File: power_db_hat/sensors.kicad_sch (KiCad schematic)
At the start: 14 parts, among them U1 INA3221

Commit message: update
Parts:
- removed R9: 0, symbol Device:R_US
- added JP1: SolderJumper_2_Open, Jumper:SolderJumper-2_P1.3mm_Open_TrianglePad1.0x1.5mm, symbol Jumper:SolderJumper_2_Open
- C3: footprint (none) -> Capacitor_SMD:C_0805_2012Metric_Pad1.18x1.45mm_HandSolder
- R32, R35, R36, R37, R38, R39, R40, R41: footprint (none) -> Resistor_SMD:R_0603_1608Metric_Pad0.98x0.95mm_HandSolder
- R33: value 10mR -> 10m; footprint (none) -> Resistor_SMD:R_2512_6332Metric_Pad1.40x3.35mm_HandSolder
- R34, R8: footprint (none) -> Resistor_SMD:R_2512_6332Metric_Pad1.40x3.35mm_HandSolder
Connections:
- net VDD: now also JP1.1 (A)
- net at U1.4 (VS): now also JP1.2 (B)
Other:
- moved on the sheet: C3
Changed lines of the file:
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@@
 	(text_box "Channel 1: 24V, 10A max (1W dissipation)\n- shunt value: 10mR\n- recommended footprint: 2512 (2W)\n\nChannel 2: 12V, 5A max (1w dissipation)\n- shunt value: 10mR\n- recommended footprint: 2512 (2W)\n\nChannel 3: 5V, 5A max (250mW dissipation)\n- shunt value 10mW\n- recommended footprint: 2512 (1W)"
 		(exclude_from_sim no)
-		(at 71.755 88.9 0)
+		(at 17.78 17.78 0)
 		(size 44.45 29.21)
 		(margins 0.9525 0.9525 0.9525 0.9525)
@@
 	(wire
 		(pts
+			(xy 71.12 43.18) (xy 72.39 43.18)
+		)
+		(stroke
+			(width 0)
+			(type default)
+		)
+	)
+	(wire
+		(pts
 			(xy 50.8 53.34) (xy 59.69 53.34)
 		)
@@
 	(wire
 		(pts
-			(xy 73.66 35.56) (xy 78.74 35.56)
+			(xy 71.12 35.56) (xy 78.74 35.56)
 		)
 		(stroke
@@
 	(hierarchical_label "VDD"
 		(shape input)
-		(at 73.66 35.56 90)
+		(at 71.12 35.56 90)
 		(effects
 			(font
@@
 	(symbol
 		(lib_id "Device:C")
-		(at 73.66 39.37 0)
+		(at 71.12 39.37 0)
 		(unit 1)
 		(exclude_from_sim no)
@@
 		(fields_autoplaced yes)
 		(property "Reference" "C3"
-			(at 77.47 38.0999 0)
+			(at 74.93 38.0999 0)
 			(effects
 				(font
@@
 		)
 		(property "Value" "100nF"
-			(at 77.47 40.6399 0)
+			(at 74.93 40.6399 0)
 			(effects
 				(font
@@
 			)
 		)
-		(property "Footprint" ""
-			(at 74.6252 43.18 0)
+		(property "Footprint" "Capacitor_SMD:C_0805_2012Metric_Pad1.18x1.45mm_HandSolder"
+			(at 72.0852 43.18 0)
 			(effects
 				(font
@@
 		)
 		(property "Datasheet" "~"
-			(at 73.66 39.37 0)
+			(at 71.12 39.37 0)
 			(effects
 				(font
@@
 		)
 		(property "Description" "Unpolarized capacitor"
-			(at 73.66 39.37 0)
+			(at 71.12 39.37 0)
 			(effects
 				(font
@@
 		)
 		(instances
-			(project ""
+			(project "power_db_hat"
 				(path "/e63e39d7-6ac0-4ffd-8aa3-1841a4541b55/fd5e5e33-5dc6-45b9-b42d-1fb287c03766/49be27b4-9dd5-4ba8-9fd8-2a64f398149b"
 					(reference "#PWR09")
@@
 			)
 		)
-		(property "Footprint" ""
+		(property "Footprint" "Resistor_SMD:R_0603_1608Metric_Pad0.98x0.95mm_HandSolder"
 			(at 126.746 54.864 90)
 			(effects
@@
 			)
 		)
-		(property "Footprint" ""
+		(property "Footprint" "Resistor_SMD:R_0603_1608Metric_Pad0.98x0.95mm_HandSolder"
 			(at 112.776 72.136 90)
 			(effects
@@
 			)
 		)
-		(property "Footprint" ""
+		(property "Footprint" "Resistor_SMD:R_0603_1608Metric_Pad0.98x0.95mm_HandSolder"
 			(at 144.526 62.484 90)
 			(effects
@@
 			)
 		)
-		(property "Footprint" ""
+		(property "Footprint" "Resistor_SMD:R_2512_6332Metric_Pad1.40x3.35mm_HandSolder"
 			(at 63.246 72.136 90)
 			(effects
@@
 			)
 		)
-		(property "Footprint" ""
+		(property "Footprint" "Resistor_SMD:R_2512_6332Metric_Pad1.40x3.35mm_HandSolder"
 			(at 63.246 56.896 90)
 			(effects
@@
 			)
 		)
-		(property "Footprint" ""
+		(property "Footprint" "Resistor_SMD:R_0603_1608Metric_Pad0.98x0.95mm_HandSolder"
 			(at 108.966 77.216 90)
 			(effects
@@
 	)
 	(symbol
+		(lib_id "Jumper:SolderJumper_2_Open")
+		(at 82.55 35.56 0)
+		(unit 1)
+		(exclude_from_sim no)
+		(in_bom no)
+		(on_board yes)
+		(dnp no)
+		(property "Reference" "JP1"
+			(at 82.55 32.004 0)
+			(effects
+				(font
+					(size 1.27 1.27)
+				)
+			)
+		)
+		(property "Value" "SolderJumper_2_Open"
+			(at 85.852 27.178 0)
+			(effects
+				(font
+					(size 1.27 1.27)
+				)
+				(hide yes)
+			)
+		)
+		(property "Footprint" "Jumper:SolderJumper-2_P1.3mm_Open_TrianglePad1.0x1.5mm"
+			(at 82.55 35.56 0)
+			(effects
+				(font
+					(size 1.27 1.27)
+				)
+				(hide yes)
+			)
+		)
+		(property "Datasheet" "~"
+			(at 82.55 35.56 0)
+			(effects
+				(font
+					(size 1.27 1.27)
+				)
+				(hide yes)
+			)
+		)
+		(property "Description" "Solder Jumper, 2-pole, open"
+			(at 82.55 35.56 0)
+			(effects
+				(font
+					(size 1.27 1.27)
+				)
+				(hide yes)
+			)
+		)
+		(pin "1"
+		)
+		(pin "2"
+		)
+		(instances
+			(project "power_db_hat"
+				(path "/e63e39d7-6ac0-4ffd-8aa3-1841a4541b55/fd5e5e33-5dc6-45b9-b42d-1fb287c03766/49be27b4-9dd5-4ba8-9fd8-2a64f398149b"
+					(reference "JP1")
+					(unit 1)
+				)
+			)
+		)
+	)
+	(symbol
 		(lib_id "power:GND")
-		(at 73.66 43.18 0)
+		(at 72.39 43.18 0)
 		(unit 1)
 		(exclude_from_sim no)
@@
 		(fields_autoplaced yes)
 		(property "Reference" "#PWR035"
-			(at 73.66 49.53 0)
+			(at 72.39 49.53 0)
 			(effects
 				(font
@@
 		)
 		(property "Value" "GND"
-			(at 73.66 48.26 0)
+			(at 72.39 48.26 0)
 			(effects
 				(font
@@
 		)
 		(property "Footprint" ""
-			(at 73.66 43.18 0)
+			(at 72.39 43.18 0)
 			(effects
 				(font
@@
 		)
 		(property "Datasheet" ""
-			(at 73.66 43.18 0)
+			(at 72.39 43.18 0)
 			(effects
 				(font
@@
 		)
 		(property "Description" "Power symbol creates a global label with name \"GND\" , ground"
-			(at 73.66 43.18 0)
+			(at 72.39 43.18 0)
 			(effects
 				(font
@@
 			)
 		)
-		(property "Footprint" ""
+		(property "Footprint" "Resistor_SMD:R_0603_1608Metric_Pad0.98x0.95mm_HandSolder"
 			(at 110.236 49.784 90)
 			(effects
@@
 			)
 		)
-		(property "Footprint" ""
+		(property "Footprint" "Resistor_SMD:R_0603_1608Metric_Pad0.98x0.95mm_HandSolder"
 			(at 153.416 65.024 90)
 			(effects
@@
 				(path "/e63e39d7-6ac0-4ffd-8aa3-1841a4541b55/fd5e5e33-5dc6-45b9-b42d-1fb287c03766/49be27b4-9dd5-4ba8-9fd8-2a64f398149b"
 					(reference "R36")
-					(unit 1)
-				)
-			)
-		)
-	)
-	(symbol
-		(lib_id "Device:R_US")
-		(at 82.55 35.56 90)
-		(unit 1)
-		(exclude_from_sim no)
-		(in_bom yes)
-		(on_board yes)
-		(dnp no)
-		(fields_autoplaced yes)
-		(property "Reference" "R9"
-			(at 82.55 29.21 90)
-			(effects
-				(font
-					(size 1.27 1.27)
-				)
-			)
-		)
-		(property "Value" "0"
-			(at 82.55 31.75 90)
-			(effects
-				(font
-					(size 1.27 1.27)
-				)
-			)
-		)
-		(property "Footprint" ""
-			(at 82.804 34.544 90)
-			(effects
-				(font
-					(size 1.27 1.27)
-				)
-				(hide yes)
-			)
-		)
-		(property "Datasheet" "~"
-			(at 82.55 35.56 0)
-			(effects
-				(font
-					(size 1.27 1.27)
-				)
-				(hide yes)
-			)
-		)
-		(property "Description" "Resistor, US symbol"
-			(at 82.55 35.56 0)
-			(effects
-				(font
-					(size 1.27 1.27)
-				)
-				(hide yes)
-			)
-		)
-		(pin "1"
-		)
-		(pin "2"
-		)
-		(instances
-			(project "power_db_hat"
-				(path "/e63e39d7-6ac0-4ffd-8aa3-1841a4541b55/fd5e5e33-5dc6-45b9-b42d-1fb287c03766/49be27b4-9dd5-4ba8-9fd8-2a64f398149b"
-					(reference "R9")
 					(unit 1)
 				)
@@
 			)
 		)
-		(property "Footprint" ""
+		(property "Footprint" "Resistor_SMD:R_0603_1608Metric_Pad0.98x0.95mm_HandSolder"
 			(at 119.126 52.324 90)
 			(effects
@@
 			)
 		)
-		(property "Value" "10mR"
+		(property "Value" "10m"
 			(at 55.88 64.77 90)
 			(effects
@@
 			)
 		)
-		(property "Footprint" ""
+		(property "Footprint" "Resistor_SMD:R_2512_6332Metric_Pad1.40x3.35mm_HandSolder"
 			(at 63.246 64.516 90)
 			(effects
@@
 			)
 		)
-		(property "Footprint" ""
+		(property "Footprint" "Resistor_SMD:R_0603_1608Metric_Pad0.98x0.95mm_HandSolder"
 			(at 134.366 57.404 90)
 			(effects

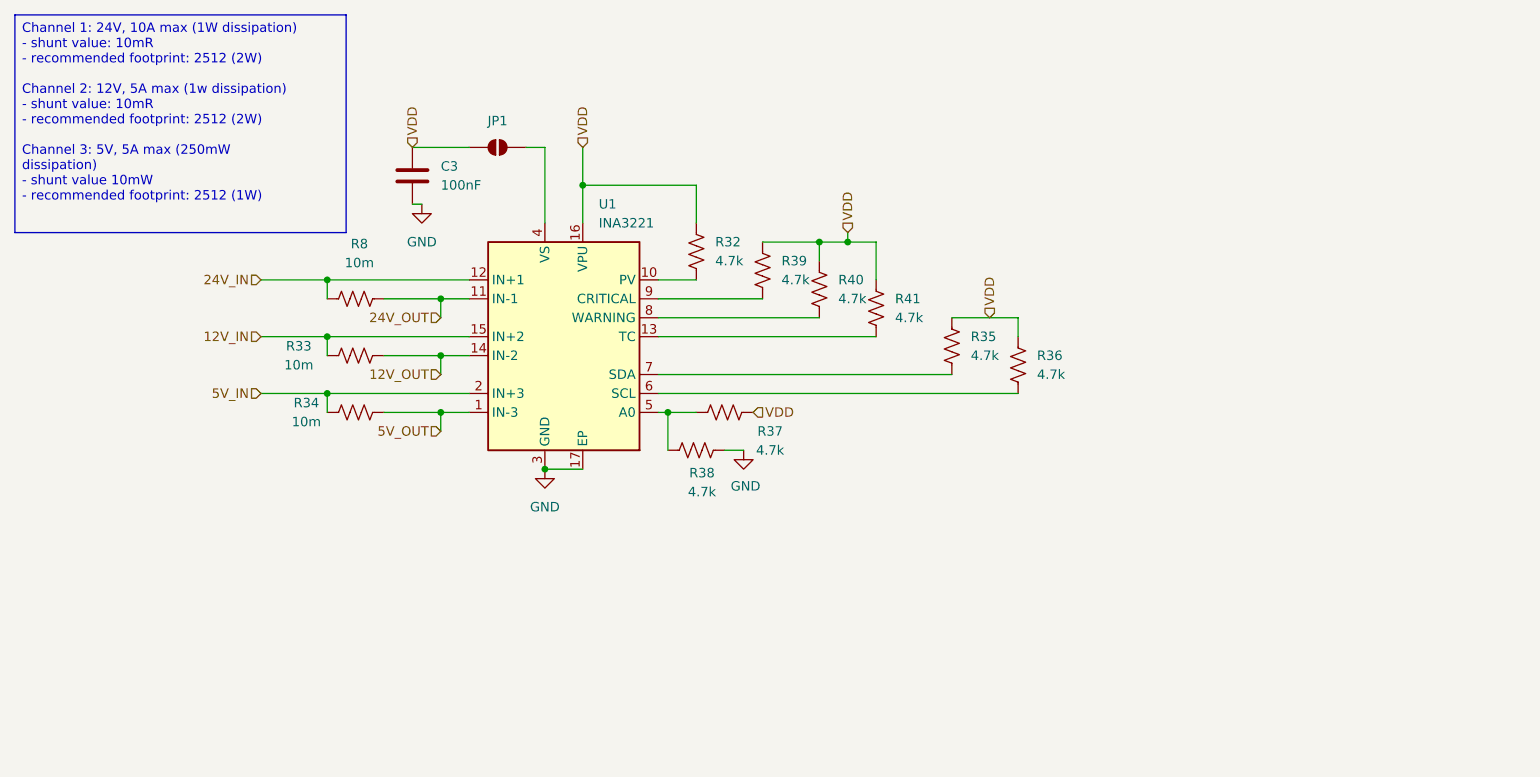
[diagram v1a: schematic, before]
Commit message: split into two PCBs
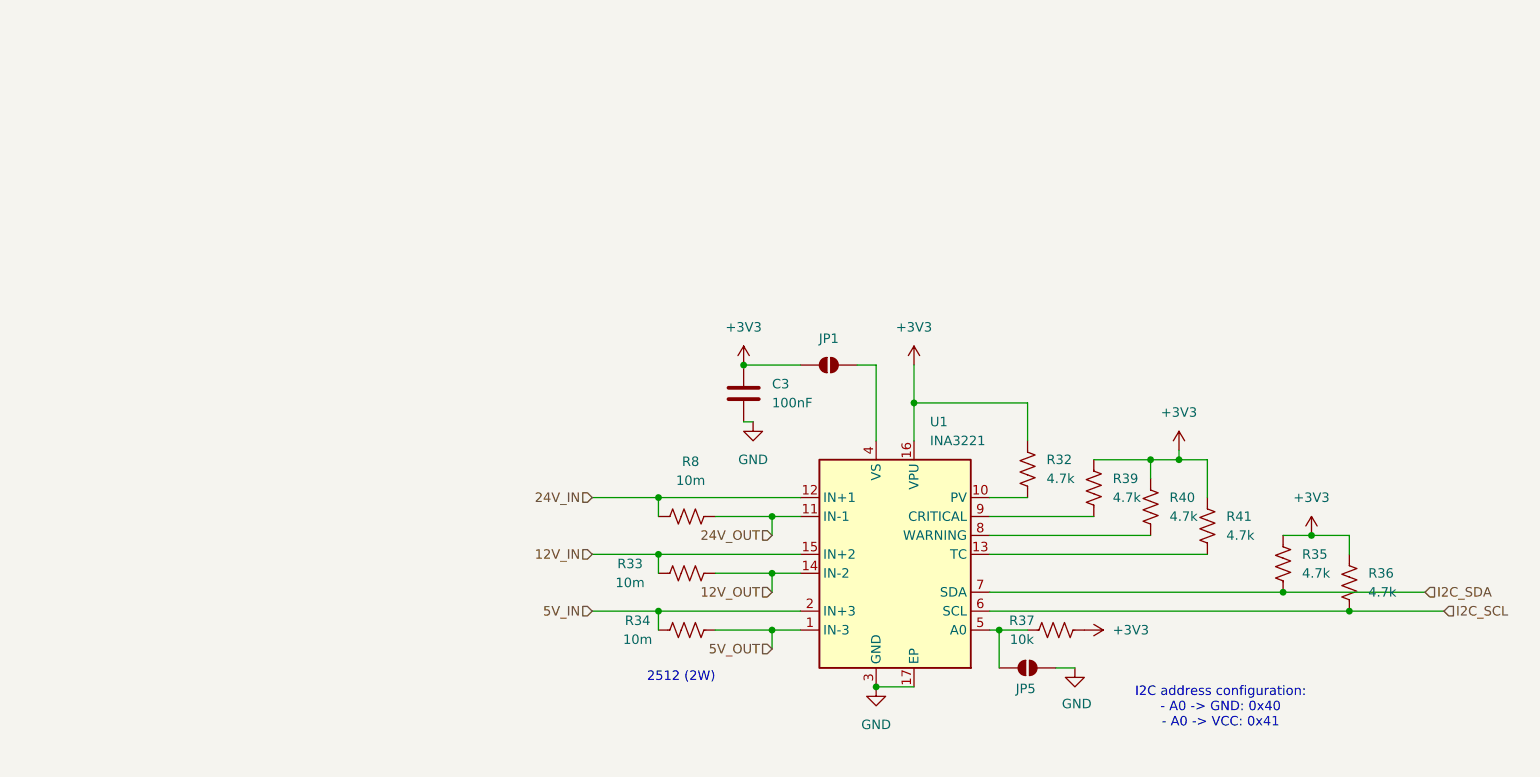
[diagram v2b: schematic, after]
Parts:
- removed R38: 4.7k, Resistor_SMD:R_0603_1608Metric_Pad0.98x0.95mm_HandSolder, symbol Device:R_US
- added JP5: SolderJumper_2_Open, Jumper:SolderJumper-2_P1.3mm_Open_TrianglePad1.0x1.5mm, symbol Jumper:SolderJumper_2_Open
- C3: footprint Capacitor_SMD:C_0805_2012Metric_Pad1.18x1.45mm_HandSolder -> Capacitor_SMD:C_0603_1608Metric_Pad1.08x0.95mm_HandSolder
- R37: value 4.7k -> 10k
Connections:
- net GND: now also JP5.2 (B)
- net at R37.2, U1.5 (A0): now also JP5.1 (A)
- net I2C_SCL: now reaches R36.2, U1.6 (SCL)
- net I2C_SDA: now reaches R35.2, U1.7 (SDA)
- net VDD renamed +3V3
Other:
- note added: "2512 (2W)"
- note added: "I2C address configuration: - A0 -> GND: 0x40 - A0 -> VCC: 0x41"
- moved on the sheet: C3, JP1, R32, R33, R34, R35, R36, R37, R39, R40, R41, R8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

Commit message: lol
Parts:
- removed R35, R36: 4.7k, Resistor_SMD:R_0603_1608Metric_Pad0.98x0.95mm_HandSolder, symbol Device:R_US

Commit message: LMAO
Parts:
- removed R33, R34: 10m, Resistor_SMD:R_2512_6332Metric_Pad1.40x3.35mm_HandSolder, symbol Device:R_US
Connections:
- net 12V_IN renamed 12V_SNS+
- net 12V_OUT renamed 12V_SNS-
- net 5V_IN renamed 5V_SNS+
- net 5V_OUT renamed 5V_SNS-
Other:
- note removed: "2512 (2W)"

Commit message: damo was here
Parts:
- removed JP1: SolderJumper_2_Open, Jumper:SolderJumper-2_P1.3mm_Open_TrianglePad1.0x1.5mm, symbol Jumper:SolderJumper_2_Open
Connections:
- net +3V3: now also U1.4 (VS)
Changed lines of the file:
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@@
-	(wire
-		(pts
-			(xy 130.81 64.77) (xy 133.35 64.77)
-		)
-		(stroke
-			(width 0)
-			(type default)
-		)
-	)
 	(wire
 		(pts
@@
 	(wire
 		(pts
-			(xy 115.57 64.77) (xy 123.19 64.77)
+			(xy 115.57 64.77) (xy 133.35 64.77)
 		)
 		(stroke
@@
 					(unit 1)
 				)
-			)
-		)
-	)
-	(symbol
-		(lib_id "Jumper:SolderJumper_2_Open")
-		(at 127 64.77 0)
-		(unit 1)
-		(body_style 1)
-		(exclude_from_sim no)
-		(in_bom no)
-		(on_board yes)
-		(in_pos_files yes)
-		(dnp no)
-		(property "Reference" "JP1"
-			(at 127 61.214 0)
-			(show_name no)
-			(do_not_autoplace no)
-			(effects
-				(font
-					(size 1.27 1.27)
-				)
-			)
-		)
-		(property "Value" "SolderJumper_2_Open"
-			(at 130.302 56.388 0)
-			(hide yes)
-			(show_name no)
-			(do_not_autoplace no)
-			(effects
-				(font
-					(size 1.27 1.27)
-				)
-			)
-		)
-		(property "Footprint" "Jumper:SolderJumper-2_P1.3mm_Open_TrianglePad1.0x1.5mm"
-			(at 127 64.77 0)
-			(hide yes)
-			(show_name no)
-			(do_not_autoplace no)
-			(effects
-				(font
-					(size 1.27 1.27)
-				)
-			)
-		)
-		(property "Datasheet" ""
-			(at 127 64.77 0)
-			(hide yes)
-			(show_name no)
-			(do_not_autoplace no)
-			(effects
-				(font
-					(size 1.27 1.27)
-				)
-			)
-		)
-		(property "Description" "Solder Jumper, 2-pole, open"
-			(at 127 64.77 0)
-			(hide yes)
-			(show_name no)
-			(do_not_autoplace no)
-			(effects
-				(font
-					(size 1.27 1.27)
-				)
-			)
-		)
-		(pin "1"
-		)
-		(pin "2"
-		)
-		(instances
-			(project "power_db_hat"
-				(path "/e63e39d7-6ac0-4ffd-8aa3-1841a4541b55/fd5e5e33-5dc6-45b9-b42d-1fb287c03766/49be27b4-9dd5-4ba8-9fd8-2a64f398149b"
-					(reference "JP1")
-					(unit 1)
-				)

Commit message: working on BOM
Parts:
- U1: footprint Package_DFN_QFN:Texas_RGV0016A_VQFN-16-1EP_4x4mm_P0.65mm_EP2.1x2.1mm -> INA3221:QFN65P400X400X100-17N-D
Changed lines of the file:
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@@
 			)
 		)
-		(property "Footprint" "Package_DFN_QFN:Texas_RGV0016A_VQFN-16-1EP_4x4mm_P0.65mm_EP2.1x2.1mm"
+		(property "Footprint" "INA3221:QFN65P400X400X100-17N-D"
 			(at 135.89 64.77 0)
 			(hide yes)
